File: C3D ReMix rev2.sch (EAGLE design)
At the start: 238 parts, among them IC1 LPC1769, IC7 74LVC1G04, Q1 BSL207SP, Q2 12MHz, SW1 SW_TACT_4P_B, SW3 SW_TACT_4P_B, T1 BC817, U3 USD-SOCKETUSD, X1 MSTBA2, X14 USBPTH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

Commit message: Almost done, but need to replace 220uF caps with SMD
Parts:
- removed U$18, U$19, U$20: FIDUCIAL, adafruit:FIDUCIAL
- removed X2: GMSTBA2, con-phoenix-762:GMSTBA2
- removed X3: GMSTBA4, con-phoenix-762:GMSTBA4
- removed X4, X5, X6, X7: 1751248, con-phoenix-350-ray:1751248
- added C15, C16: (no value), resistor:CPOL-EU153CLV-0810
- added X8: 1751303, con-phoenix-350-ray:1751303
- added X9: GMSTBA6, con-phoenix-762:GMSTBA6
- C1, C11, C12, C51, C6, C65: value .1uF -> 104
- C23, C24: value 100u -> 100uF
- D2: value (none) -> SS34
- IC2: value (none) -> LM2596-5
- LED10, LED11, LED8: value LED -> RED
- LED5: device led:LEDCHIP-LED0603 -> led:LEDSML0603
- LED6, LED7: value (none) -> RED
- R1, R10, R11, R12, R13, R14, R15, R17, R18, R2, R3, R53, R77, R8, R9: device resistor:R-US_R0603 -> resistor:R-EU_R0603
- R16, R28, R29, R31, R4: device adafruit:R-US_R0603 -> resistor:R-EU_R0603
- R20, R34, R39, R50, R52: value 10k -> 10K
- R21, R22, R23, R24, R5, R6: value 10k -> 10K; device adafruit:R-US_R0603 -> resistor:R-EU_R0603
- R57: value 1.5K -> 1.5k
- R7: value 1.5K -> 1.5k; device resistor:R-US_R0603 -> resistor:R-EU_R0603
- U1: value (none) -> 1117-3.3
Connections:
- net 24V: now also X9-1.1; no longer X2-1.1
- net E1-CONTROL: now also X8-2.K; no longer X4-2.K
- net E2-CONTROL: now also X8-4.K; no longer X5-2.K
- net E3-CONTROL: now also X8-6.K; no longer X6-2.K
- net E4-CONTROL: now also X8-8.K; no longer X7-2.K
- net GND: now also X9-2.1, X9-4.1; no longer X2-2.1, X3-2.1
- net HEATBED-CONTROL: now also X9-6.1; no longer X3-4.1
- net HEATBEDVIN: now also X9-3.1, X9-5.1; no longer X3-1.1, X3-3.1
- net HEATERVIN: now also X8-1.K, X8-3.K, X8-5.K, X8-7.K; no longer X4-1.K, X5-1.K, X6-1.K, X7-1.K

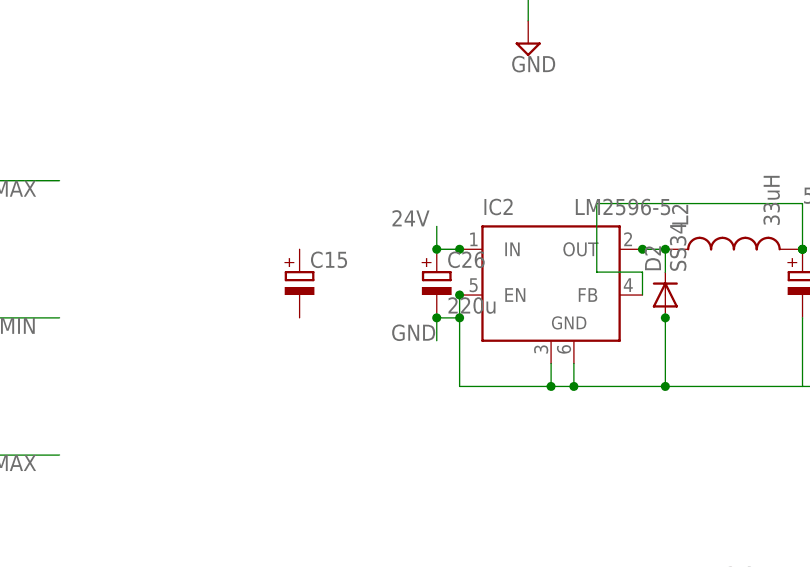
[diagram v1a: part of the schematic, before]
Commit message: 1/2 Cap 220uF Converted
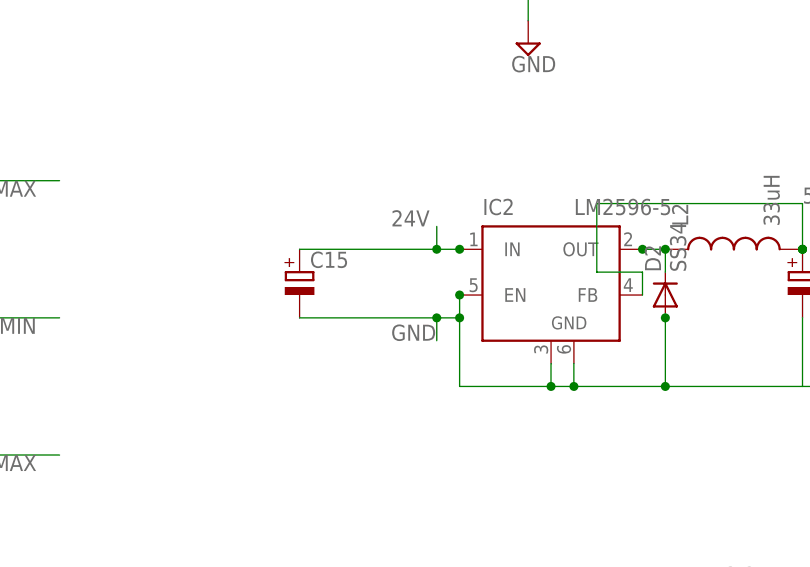
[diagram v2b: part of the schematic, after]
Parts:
- removed C26: 220u, rcl:CPOL-EUE2.5-7
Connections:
- net 24V: now also C15.+; no longer C26.+
- net GND: now also C15.-; no longer C26.-
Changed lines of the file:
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@@
 <part name="L2" library="SparkFun-Passives" deviceset="INDUCTOR" device="PWR" value="33uH"/>
 <part name="D2" library="dp_devices" deviceset="DIODE" device="-DO-214AC" value="SS34"/>
-<part name="C26" library="rcl" deviceset="CPOL-EU" device="E2.5-7" value="220u"/>
 <part name="C27" library="rcl" deviceset="CPOL-EU" device="E2.5-7" value="220u"/>
 <part name="D3" library="microbuilder" deviceset="DIODE" device="SMA" value="MBRA210LT3"/>
@@
 <instance part="L2" gate="G$1" x="317.5" y="325.12" rot="R90"/>
 <instance part="D2" gate="D" x="309.88" y="320.04" rot="R90"/>
-<instance part="C26" gate="G$1" x="284.48" y="322.58"/>
 <instance part="C27" gate="G$1" x="325.12" y="322.58"/>
 <instance part="D3" gate="G$1" x="274.32" y="370.84"/>
@@
 <junction x="309.88" y="317.5"/>
 <junction x="309.88" y="309.88"/>
-<pinref part="C26" gate="G$1" pin="-"/>
 <junction x="284.48" y="317.5"/>
 <pinref part="C27" gate="G$1" pin="-"/>
@@
 <wire x1="325.12" y1="309.88" x2="327.66" y2="309.88" width="0.1524" layer="91"/>
 <wire x1="325.12" y1="317.5" x2="325.12" y2="309.88" width="0.1524" layer="91"/>
+<pinref part="C15" gate="G$1" pin="-"/>
+<wire x1="284.48" y1="317.5" x2="269.24" y2="317.5" width="0.1524" layer="91"/>
 </segment>
 <segment>
@@
 <wire x1="284.48" y1="325.12" x2="284.48" y2="327.66" width="0.1524" layer="91"/>
 <junction x="287.02" y="325.12"/>
-<pinref part="C26" gate="G$1" pin="+"/>
 <junction x="284.48" y="325.12"/>
+<pinref part="C15" gate="G$1" pin="+"/>
+<wire x1="284.48" y1="325.12" x2="269.24" y2="325.12" width="0.1524" layer="91"/>
 </segment>
 <segment>

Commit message: Rev2, Huge Amount of stuff added
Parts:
- removed C27: 220u, rcl:CPOL-EUE2.5-7
- added R56: 10k, resistor:R-EU_R0603
- C15, C16: value (none) -> 220uF
- U$13, U$14, U$15, U$16: value IRLR024 -> SUD50N04
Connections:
- net USB_D+ renamed USB_P
- net USB_D- renamed USB_N
- net 5V: now also R56.2
- net 5VREG: now also C16.+; no longer C27.+
- net GND: now also C16.-; no longer C27.-
- net N$56: now also R56.1
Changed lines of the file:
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@@
 <layer number="250" name="Descript" color="3" fill="1" visible="no" active="no"/>
 <layer number="251" name="SMDround" color="12" fill="11" visible="no" active="no"/>
+<layer number="252" name="BR-BS" color="4" fill="9" visible="yes" active="yes"/>
+<layer number="253" name="BR-LS" color="1" fill="2" visible="yes" active="yes"/>
 <layer number="254" name="cooling" color="7" fill="1" visible="yes" active="yes"/>
 <layer number="255" name="routoute" color="7" fill="1" visible="yes" active="yes"/>
@@
 <part name="L2" library="SparkFun-Passives" deviceset="INDUCTOR" device="PWR" value="33uH"/>
 <part name="D2" library="dp_devices" deviceset="DIODE" device="-DO-214AC" value="SS34"/>
-<part name="C27" library="rcl" deviceset="CPOL-EU" device="E2.5-7" value="220u"/>
 <part name="D3" library="microbuilder" deviceset="DIODE" device="SMA" value="MBRA210LT3"/>
 <part name="5VREG" library="SparkFun" deviceset="5V" device="" value="5vreg"/>
@@
 <part name="JP10" library="SparkFun-Connectors" deviceset="M04" device="LOCK"/>
 <part name="U$12" library="adafruit" deviceset="FIDUCIAL" device=""/>
-<part name="U$13" library="Cohesion_parts" deviceset="N-POWER-MOSFET" device="DPAK-MOSFET" value="IRLR024"/>
+<part name="U$13" library="Cohesion_parts" deviceset="N-POWER-MOSFET" device="DPAK-MOSFET" value="SUD50N04"/>
 <part name="R35" library="resistor" deviceset="R-EU_" device="R0603" value="10r"/>
 <part name="R36" library="resistor" deviceset="R-EU_" device="R0603" value="100k"/>
@@
 <part name="SUPPLY5" library="supply2" deviceset="GND" device=""/>
 <part name="RN2" library="resistor-dil" deviceset="4R-N" device="0603-ARV" value="4k7"/>
-<part name="U$14" library="Cohesion_parts" deviceset="N-POWER-MOSFET" device="DPAK-MOSFET" value="IRLR024"/>
+<part name="U$14" library="Cohesion_parts" deviceset="N-POWER-MOSFET" device="DPAK-MOSFET" value="SUD50N04"/>
 <part name="R40" library="resistor" deviceset="R-EU_" device="R0603" value="10r"/>
 <part name="R41" library="resistor" deviceset="R-EU_" device="R0603" value="100k"/>
@@
 <part name="LED8" library="led" deviceset="LED" device="SML0603" value="RED"/>
 <part name="R42" library="resistor" deviceset="R-EU_" device="R0603" value="1.5k"/>
-<part name="U$15" library="Cohesion_parts" deviceset="N-POWER-MOSFET" device="DPAK-MOSFET" value="IRLR024"/>
+<part name="U$15" library="Cohesion_parts" deviceset="N-POWER-MOSFET" device="DPAK-MOSFET" value="SUD50N04"/>
 <part name="R43" library="resistor" deviceset="R-EU_" device="R0603" value="10r"/>
 <part name="R44" library="resistor" deviceset="R-EU_" device="R0603" value="100k"/>
@@
 <part name="LED10" library="led" deviceset="LED" device="SML0603" value="RED"/>
 <part name="R45" library="resistor" deviceset="R-EU_" device="R0603" value="1.5k"/>
-<part name="U$16" library="Cohesion_parts" deviceset="N-POWER-MOSFET" device="DPAK-MOSFET" value="IRLR024"/>
+<part name="U$16" library="Cohesion_parts" deviceset="N-POWER-MOSFET" device="DPAK-MOSFET" value="SUD50N04"/>
 <part name="R46" library="resistor" deviceset="R-EU_" device="R0603" value="10r"/>
 <part name="R47" library="resistor" deviceset="R-EU_" device="R0603" value="100k"/>
@@
 <part name="X8" library="con-phoenix-350-ray" deviceset="1751303" device=""/>
 <part name="X9" library="con-phoenix-762" deviceset="GMSTBA6" device=""/>
-<part name="C15" library="resistor" deviceset="CPOL-EU" device="153CLV-0810"/>
-<part name="C16" library="resistor" deviceset="CPOL-EU" device="153CLV-0810"/>
+<part name="C15" library="resistor" deviceset="CPOL-EU" device="153CLV-0810" value="220uF"/>
+<part name="C16" library="resistor" deviceset="CPOL-EU" device="153CLV-0810" value="220uF"/>
+<part name="R56" library="resistor" deviceset="R-EU_" device="R0603" value="10k"/>
 </parts>
 <sheets>
@@
 <instance part="L2" gate="G$1" x="317.5" y="325.12" rot="R90"/>
 <instance part="D2" gate="D" x="309.88" y="320.04" rot="R90"/>
-<instance part="C27" gate="G$1" x="325.12" y="322.58"/>
 <instance part="D3" gate="G$1" x="274.32" y="370.84"/>
 <instance part="5VREG" gate="G$1" x="269.24" y="393.7"/>
@@
 <instance part="C15" gate="G$1" x="269.24" y="322.58"/>
 <instance part="C16" gate="G$1" x="337.82" y="322.58"/>
+<instance part="R56" gate="G$1" x="530.86" y="137.16"/>
 </instances>
 <busses>
@@
 <junction x="309.88" y="309.88"/>
 <junction x="284.48" y="317.5"/>
-<pinref part="C27" gate="G$1" pin="-"/>
 <wire x1="309.88" y1="309.88" x2="325.12" y2="309.88" width="0.1524" layer="91"/>
 <wire x1="325.12" y1="309.88" x2="327.66" y2="309.88" width="0.1524" layer="91"/>
@@
 <pinref part="C15" gate="G$1" pin="-"/>
 <wire x1="284.48" y1="317.5" x2="269.24" y2="317.5" width="0.1524" layer="91"/>
+<pinref part="C16" gate="G$1" pin="-"/>
+<wire x1="337.82" y1="317.5" x2="325.12" y2="317.5" width="0.1524" layer="91"/>
 </segment>
 <segment>
@@
 </segment>
 </net>
-<net name="USB_D-" class="0">
+<net name="USB_N" class="0">
 <segment>
 <wire x1="129.54" y1="149.86" x2="50.8" y2="149.86" width="0.1524" layer="91"/>
@@
 </segment>
 </net>
-<net name="USB_D+" class="0">
+<net name="USB_P" class="0">
 <segment>
 <wire x1="48.26" y1="152.4" x2="58.42" y2="152.4" width="0.1524" layer="91"/>
@@
 <wire x1="530.86" y1="160.02" x2="530.86" y2="147.32" width="0.1524" layer="91"/>
 <junction x="530.86" y="147.32"/>
+<pinref part="R56" gate="G$1" pin="2"/>
+<wire x1="535.94" y1="137.16" x2="535.94" y2="147.32" width="0.1524" layer="91"/>
+<junction x="535.94" y="147.32"/>
 </segment>
 <segment>
@@
 <wire x1="302.26" y1="330.2" x2="325.12" y2="330.2" width="0.1524" layer="91"/>
 <wire x1="325.12" y1="330.2" x2="325.12" y2="325.12" width="0.1524" layer="91"/>
-<pinref part="C27" gate="G$1" pin="+"/>
 <junction x="325.12" y="325.12"/>
+<pinref part="C16" gate="G$1" pin="+"/>
+<wire x1="337.82" y1="325.12" x2="325.12" y2="325.12" width="0.1524" layer="91"/>
 </segment>
 <segment>
@@
 </segment>
 </net>
-<net name="N$56" class="0">
-<segment>
-<pinref part="T1" gate="G$1" pin="C"/>
-<pinref part="JP13" gate="G$1" pin="2"/>
-<wire x1="518.16" y1="142.24" x2="518.16" y2="149.86" width="0.1524" layer="91"/>
-<wire x1="535.94" y1="149.86" x2="518.16" y2="149.86" width="0.1524" layer="91"/>
-<pinref part="D14" gate="G$1" pin="A"/>
-<wire x1="518.16" y1="149.86" x2="515.62" y2="149.86" width="0.1524" layer="91"/>
-<junction x="518.16" y="149.86"/>
-<pinref part="D16" gate="G$1" pin="A"/>
-<wire x1="515.62" y1="149.86" x2="510.54" y2="149.86" width="0.1524" layer="91"/>
-<junction x="515.62" y="149.86"/>
-</segment>
-</net>
 <net name="V-ENDSTOP" class="0">
 <segment>
@@
 </segment>
 </net>
+<net name="N$56" class="0">
+<segment>
+<pinref part="R56" gate="G$1" pin="1"/>
+<wire x1="525.78" y1="137.16" x2="523.24" y2="137.16" width="0.1524" layer="91"/>
+<wire x1="523.24" y1="137.16" x2="523.24" y2="142.24" width="0.1524" layer="91"/>
+<pinref part="T1" gate="G$1" pin="C"/>
+<pinref part="JP13" gate="G$1" pin="2"/>
+<wire x1="518.16" y1="142.24" x2="518.16" y2="149.86" width="0.1524" layer="91"/>
+<wire x1="535.94" y1="149.86" x2="518.16" y2="149.86" width="0.1524" layer="91"/>
+<pinref part="D14" gate="G$1" pin="A"/>
+<wire x1="518.16" y1="149.86" x2="515.62" y2="149.86" width="0.1524" layer="91"/>
+<junction x="518.16" y="149.86"/>
+<pinref part="D16" gate="G$1" pin="A"/>
+<wire x1="515.62" y1="149.86" x2="510.54" y2="149.86" width="0.1524" layer="91"/>
+<junction x="515.62" y="149.86"/>
+<wire x1="523.24" y1="142.24" x2="518.16" y2="142.24" width="0.1524" layer="91"/>
+<junction x="518.16" y="142.24"/>
+</segment>
+</net>
